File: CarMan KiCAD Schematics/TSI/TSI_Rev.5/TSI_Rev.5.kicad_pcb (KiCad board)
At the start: 2 copper layers, 203.2 x 165.1 mm, 255 parts, among them IC1 TS431ILT, IC4 TS431ILT, J1 J1, J10 J10, J11 J11, J12 J12, J13 Conn_01x01, J13.1 Conn_01x06, J13.2 Conn_01x06, J14 J14, J15 J15, J16 J16, J17 J17, J18 J18, J19 J19, J2 Current_Sensor, J20 J20, J21 J21, J22 J22, J23 J23, J24 Conn_01x01, J25 Conn_01x01, J26 J26, J27 J27, J28 Conn_01x01, J29 J29, J3 J3, J4 J4, J5 J5, J6 J6, J7 J7, J8 J8, J9 J9, K1 APAN3105, K2 G5LE-1-E, K3 SFS2-DC24V, K4 SFS2-DC24V, Q1 ZVP1320F, Q11 TN2130K1-G, Q2 MMBF170, Q3 ZVP1320F, Q5 SI1302DL-T1-E3, SW1 TS5A3159DBVT, U1 RDE03110S12, U10 MC7805BDTRKG, U11 TLP293, U12 REF3033, U13 TLP293, U14 Bottom Left, U15 Top Left, U16 TS372CDT, U17 Top Right, U18 MCP6004, U19 74HC00, U2 Bottom Right, U21 MCP6004, U22 MCP23016-I_SO, U23 DAC5574IDGS, U24 TLP293, U25 NCD9830DBR2G, U26 MCP6004, U29 SN74LVC1G08DCKR, U3 TS912, U30 TLP293, U31 TLP293, U32 TLP293, U34 TLP293, U35 MCP6004, U37 TLP293, U4 ACPL-C870, U40 MCP6004, U41 PDQ10-Q24-D5-D, U42 LT1763CS8-3.3PBF, U48 TLP293, U49 TLP293, U5 SI8600AB-B-IS, U6 TS912, U7 MCP6004, U8 74ACT11030, U9 STN3NF06L

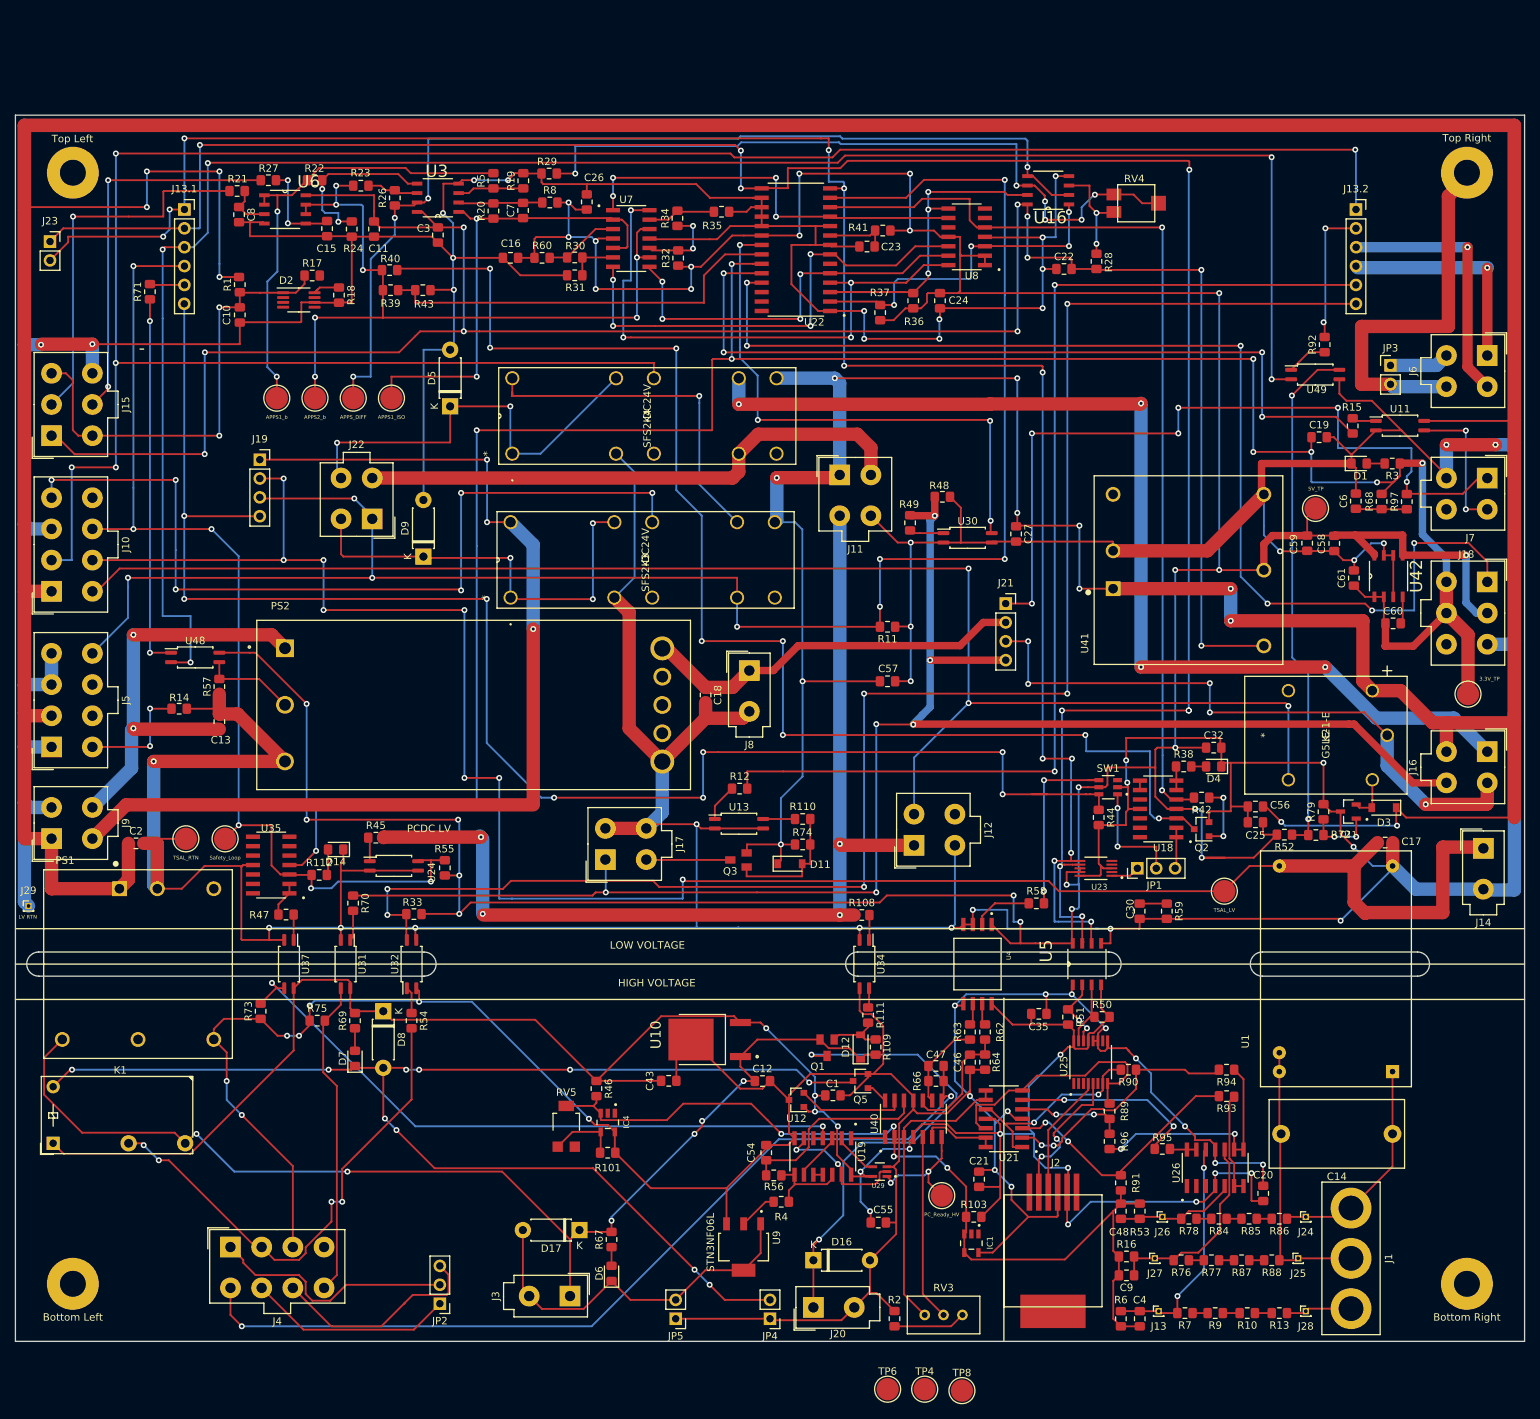
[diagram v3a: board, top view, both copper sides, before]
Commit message: TSI (~99%) - Confirmed TSI pin headers and logic pin header alignment - Divided board into several sections - Placed TSV testing pads and made last connection
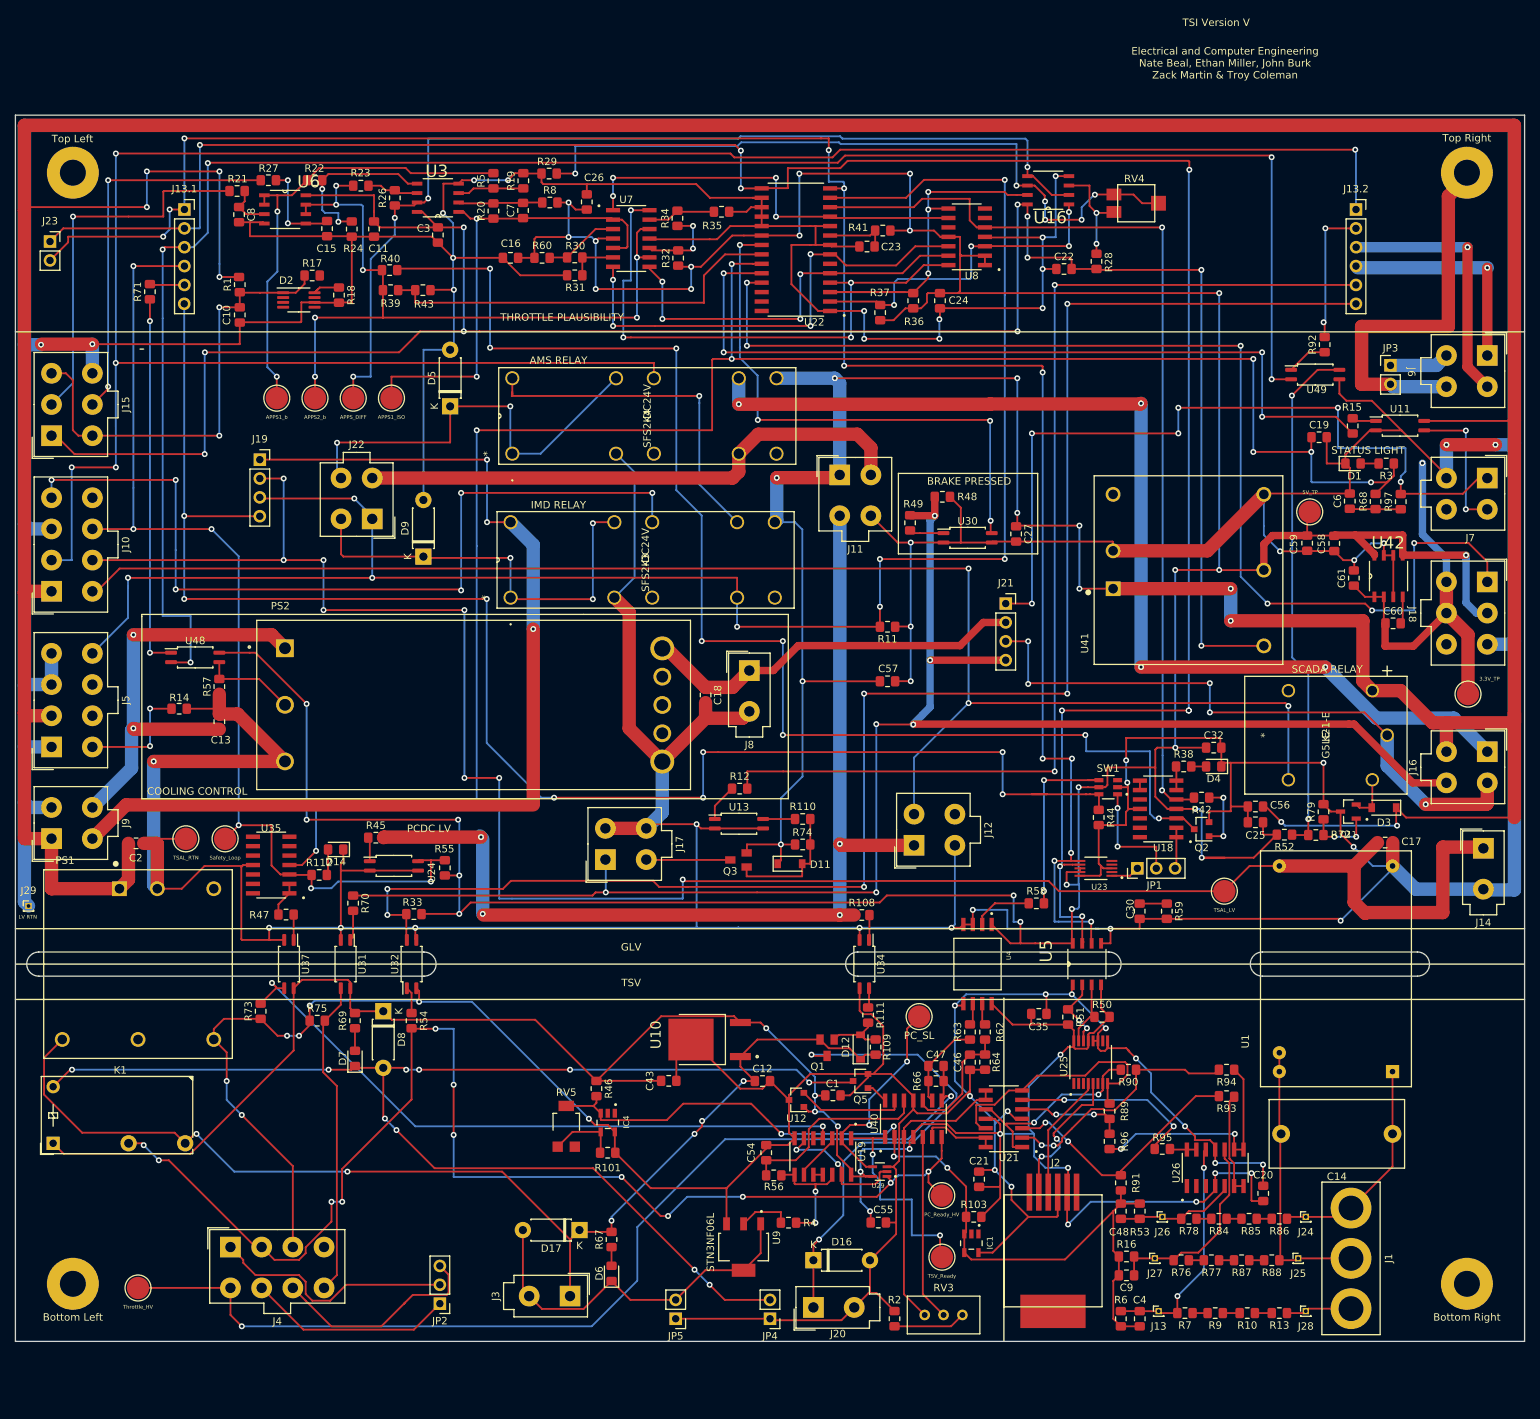
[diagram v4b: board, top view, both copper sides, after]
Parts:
- moved TP8 111.8 mm to (156.4, 201.8)
- moved TP6 50.3 mm to (261.6, 165.2)
- moved TP4 17.9 mm to (264.7, 197.6)
- moved R4 2.98 mm to (244.0, 193.0)
- moved TP10 0.91 mm to (314.2, 97.3)
- moved R3 0.81 mm to (324.5, 90.7)
- moved R97 0.81 mm to (326.4, 95.9)
- moved C6 0.81 mm to (319.6, 95.8)
- moved D1 0.81 mm to (320.0, 90.7)
- moved R68 0.81 mm to (323.1, 95.9)
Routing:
- net /PCDC_Circuit/PC_Ready_HV: track 16.2 -> 104.2 mm, vias 2 -> 8
- net /PCDC_Circuit/TSV_Ready: track 4.64 -> 29.2 mm, vias 0 -> 2
- net /PCDC_Circuit/PC_AND_SL_READY: track 6.10 -> 28.3 mm, vias 0 -> 2
- net /Throttle_HV: track 120.4 -> 137.1 mm
- net Net-(R4-Pad2): track 11.7 -> 16.8 mm, vias 0 -> 2
- net /3.3V: track 315.5 -> 311.7 mm
- net Net-(R4-Pad1): track 5.28 -> 7.11 mm
- net /AIRS-: track 1485.8 -> 1484.1 mm
- net /5HV: track 312.9 -> 314.5 mm
- net /5V: track 543.7 -> 542.9 mm
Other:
- board text added: "AMS RELAY"
- board text added: "BRAKE PRESSED"
- board text added: "COOLING CONTROL"
- board text added: "Electrical and Computer Engineering Nate Beal, Ethan Miller, John Burk Zack Martin & Troy Coleman"
- board text added: "GLV"
- board text added: "IMD RELAY"
- board text added: "J18"
- board text added: "J6"
- board text added: "SCADA RELAY"
- board text added: "STATUS LIGHT"
- board text added: "THROTTLE PLAUSIBILITY"
- board text added: "TSI Version V"
- board text added: "TSV"
- board text added: "Zacky Bear Doesn't Like"
- board text removed: "HIGH VOLTAGE"
- board text removed: "LOW VOLTAGE"

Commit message: Updated board, added silk art
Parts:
- added G***: LOGO, TSI_Rev_2021_Footprint_Lib:logo_lafayette_ece_medium_24mmx9mm, F.Cu at (114.4, 200.5)
- R1: value 1K -> 76K
- moved J28 40.7 mm to (273.9, 213.9)
- moved R38 40.7 mm to (257.5, 140.6)
- moved C17 40.7 mm to (284.6, 150.8)
- moved C58 40.7 mm to (277.8, 110.5)
- moved C6 40.7 mm to (279.8, 104.8)
- moved D3 40.7 mm to (284.4, 146.1)
- moved J1 40.7 mm to (280.0, 206.8)
- moved J24 40.7 mm to (273.9, 201.2)
- moved JP3 40.7 mm to (285.3, 86.6)
- moved Q2 40.7 mm to (259.9, 149.0)
- moved R42 40.7 mm to (259.9, 144.7)
- moved R52 40.7 mm to (271.0, 149.7)
- moved R7 40.7 mm to (257.6, 214.1)
- moved R77 40.7 mm to (261.2, 207.0)
- moved R95 40.7 mm to (254.6, 192.0)
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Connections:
- U25 pad 10: Net-(U25-Pad10) -> /5HV
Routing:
- net /5V_ISO_RTN: vias 5 -> 7
- net /AMS_FAULT_LED: vias 5 -> 6
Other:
- board text added: "TSI Version V Nate Beal, Ethan Miller, John Burk Zack Martin & Troy Coleman"
- board text removed: "Electrical and Computer Engineering Nate Beal, Ethan Miller, John Burk Zack Martin & Troy Coleman"
- board text removed: "TSI Version V"

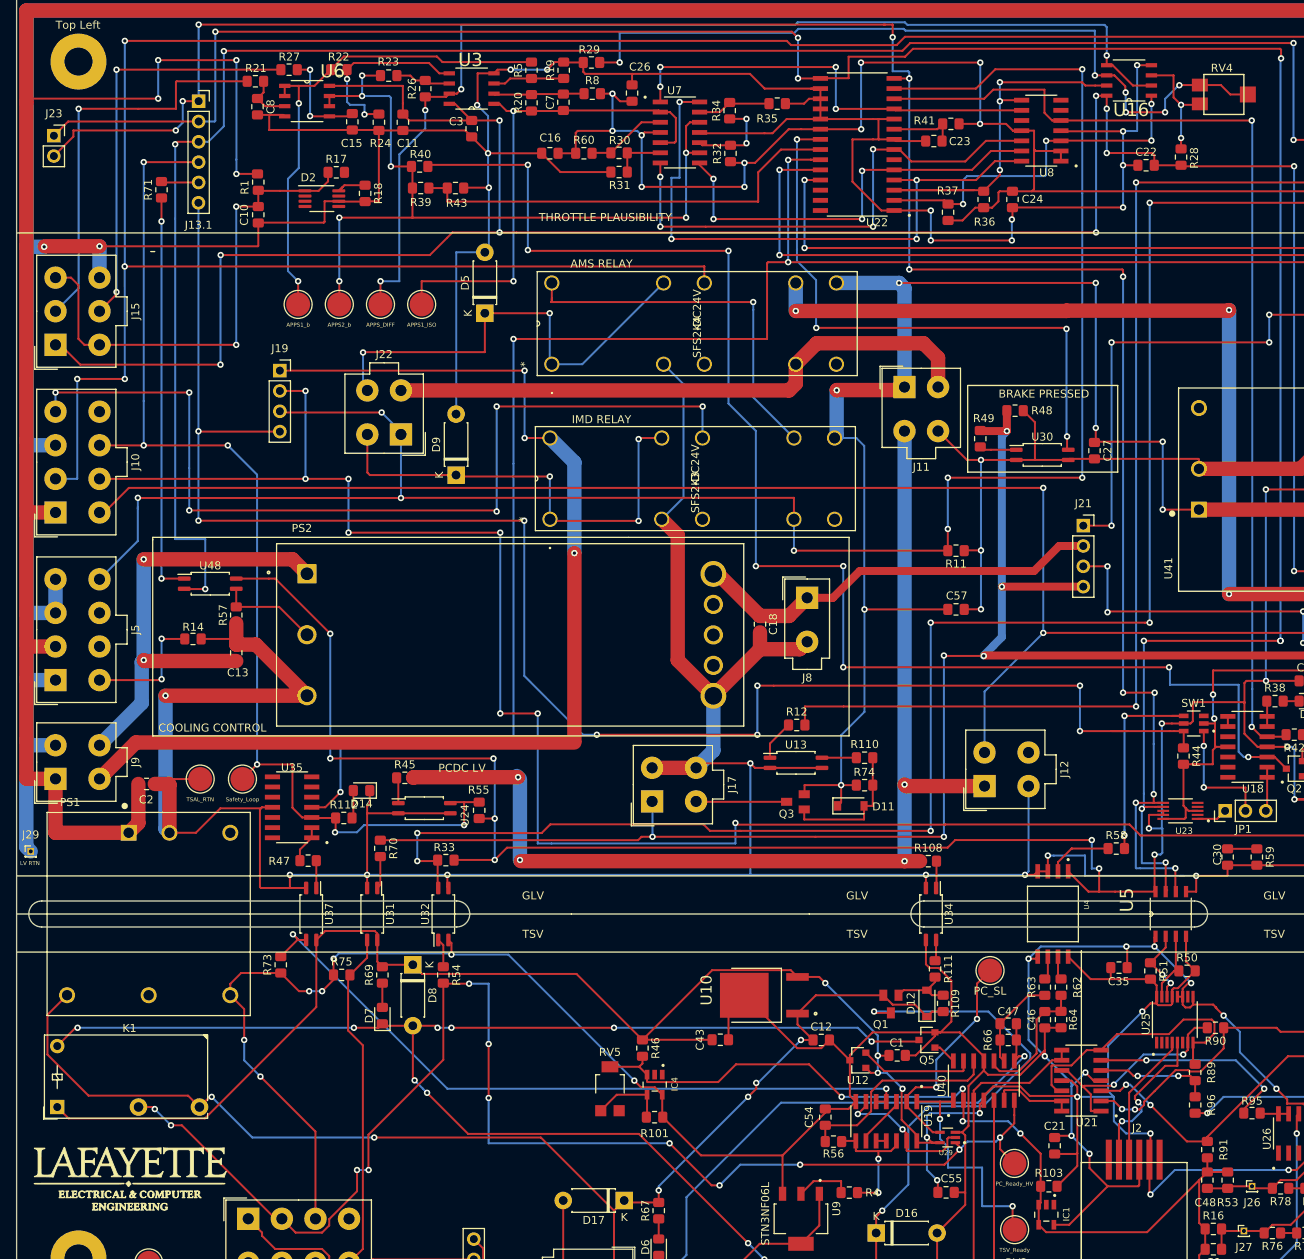
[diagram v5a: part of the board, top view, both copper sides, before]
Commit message: TSI (99.5%) - Updated footprints on pcb
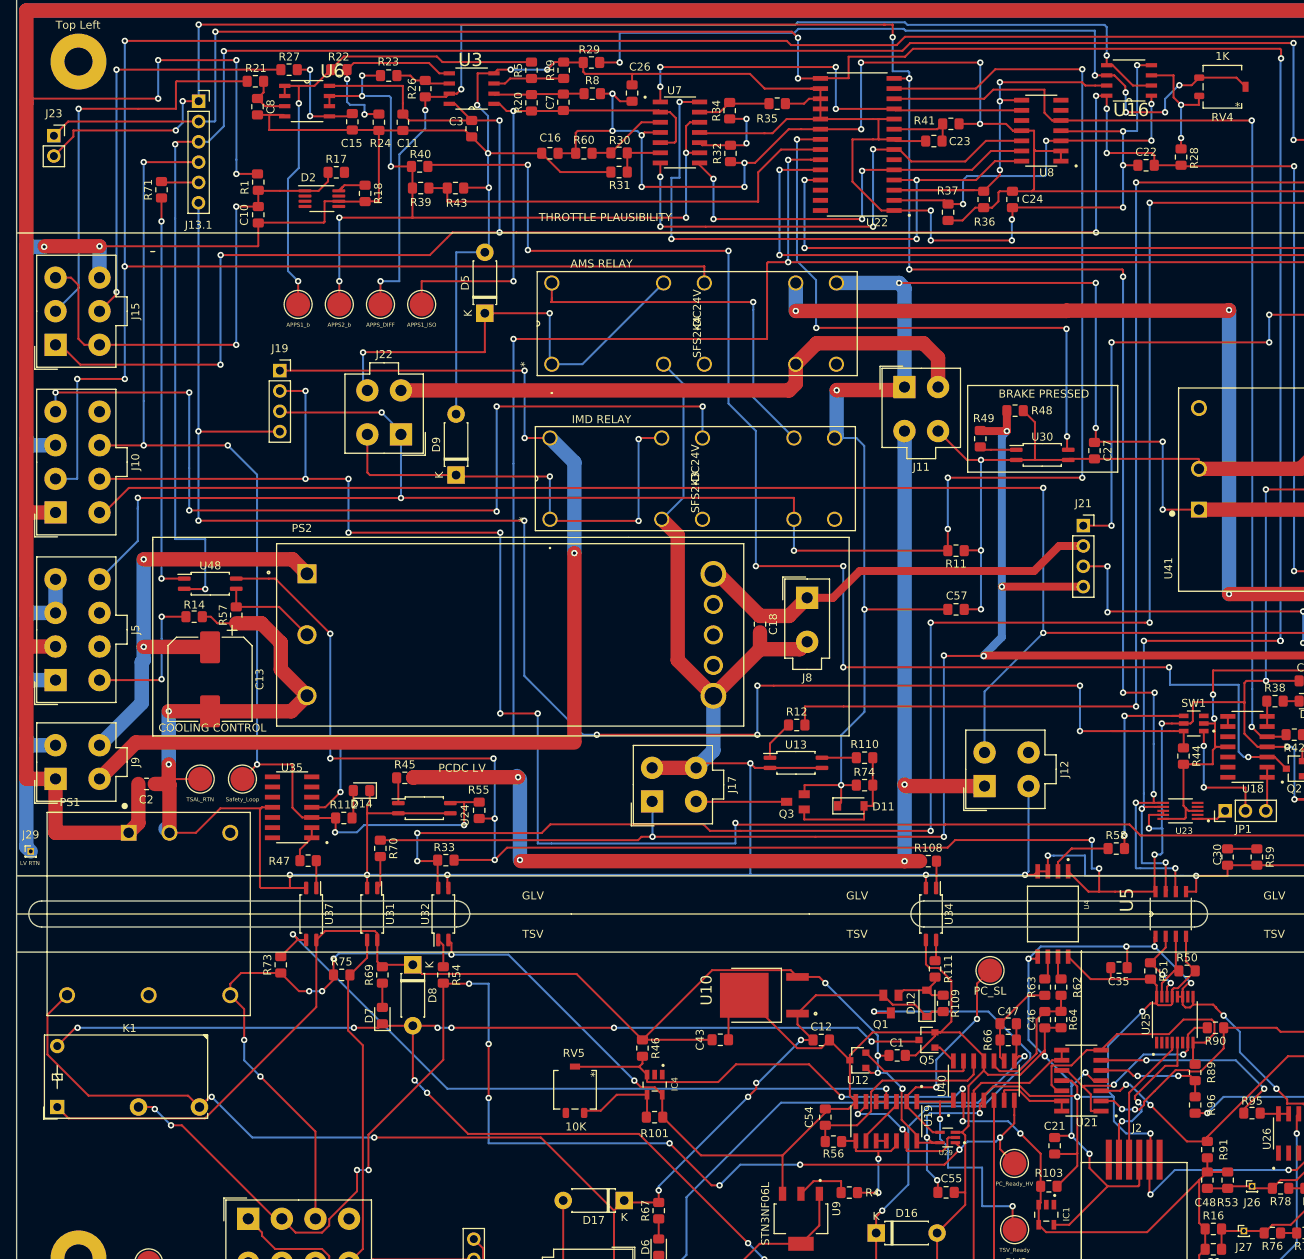
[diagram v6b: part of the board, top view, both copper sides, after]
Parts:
- removed G***: LOGO, TSI_Rev_2021_Footprint_Lib:logo_lafayette_ece_medium_24mmx9mm
- C13: value 100u -> 100uF; footprint Capacitor_SMD:C_0805_2012Metric_Pad1.15x1.40mm_HandSolder -> Capacitor_SMD:CP_Elec_10x10
- R38, R47, R69: value 500 -> 499
- RV4: footprint TSI_Rev_2021_Footprint_Lib:trim_pot -> TSI_Rev_2021_Footprint_Lib:Potentiometer
- RV5: value R_POT_TRIM -> 10K; footprint TSI_Rev_2021_Footprint_Lib:23BR10KLFTR -> TSI_Rev_2021_Footprint_Lib:Potentiometer
- moved C13 4.66 mm to (124.4, 137.8), turned to 270 degrees
- moved RV5 4.37 mm to (170.0, 189.1), turned to 270 degrees
- moved R14 2.78 mm to (122.4, 130.0)
- moved RV4 0.98 mm to (250.9, 63.8), turned to 180 degrees
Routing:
- net /AIRS-: track 1484.0 -> 1477.1 mm, vias 37 -> 38
- net /1.24V_REF: track 122.8 -> 127.1 mm
- net /COOL_24V: track 58.3 -> 55.0 mm
- net /IMD_MHS: track 15.8 -> 18.7 mm
- net Net-(IC4-Pad4): track 9.46 -> 11.7 mm
- net Net-(R28-Pad2): track 14.7 -> 15.7 mm
